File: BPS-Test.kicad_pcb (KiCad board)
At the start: 2 copper layers, 99 x 94 mm, 128 parts, among them J1 Conn_01x02, J10 Conn_01x02, J11 Conn_01x02, J12 Conn_01x02, J13 Conn_01x02, J14 Conn_01x02, J15 Conn_01x02, J16 Conn_01x02, J17 Conn_01x02, J18 Conn_01x02, J19 Conn_01x02, J2 Conn_01x02, J20 Conn_01x02, J21 Conn_01x02, J22 Conn_01x02, J23 Conn_01x07, J24 Conn_01x07, J25 Conn_01x01, J26 Conn_01x01, J3 Conn_01x02, J4 Conn_01x02, J5 Conn_01x02, J6 Conn_01x02, J7 Conn_01x02, J8 Conn_01x02, J9 Conn_01x02, T1 Transformer_1P_1S, T2 Transformer_1P_1S, U1 LM5180QNGURQ1, U2 LM5180QNGURQ1

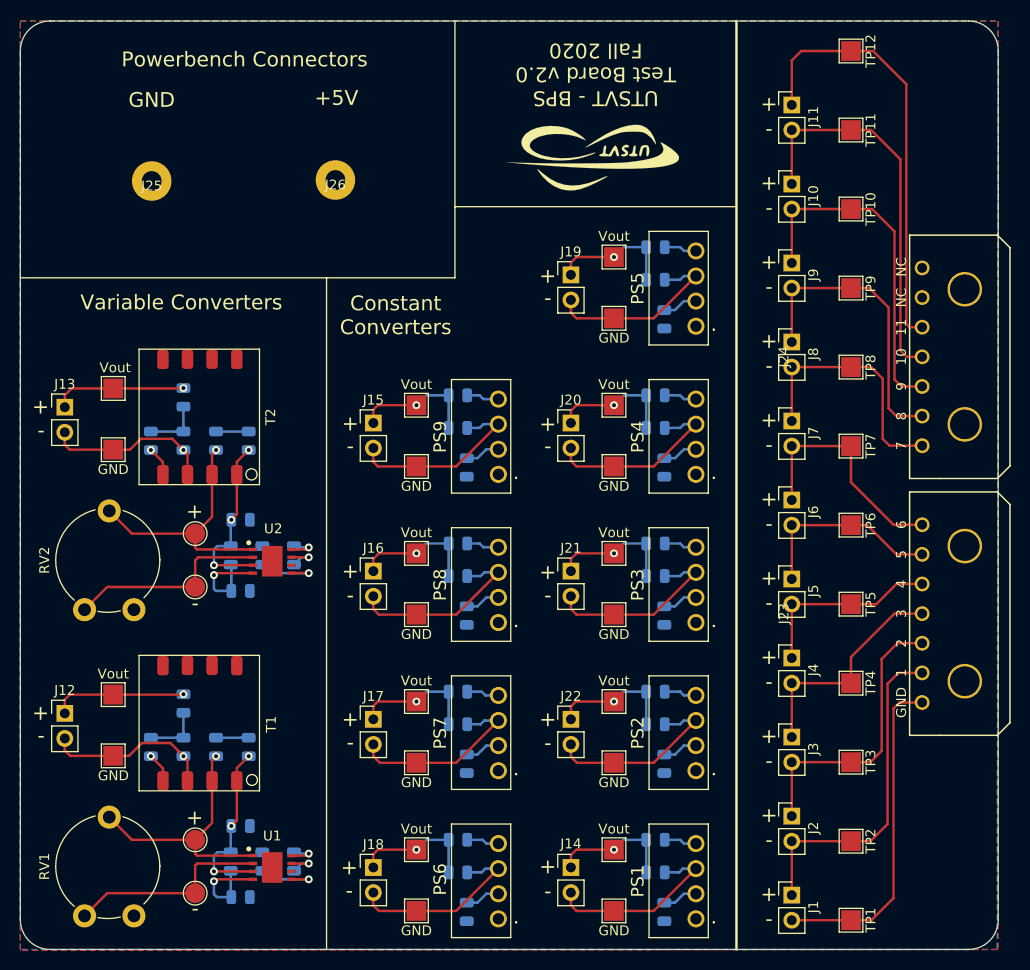
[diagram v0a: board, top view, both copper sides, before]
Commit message: Cleans up repo by adding symbols and footprints to the common library
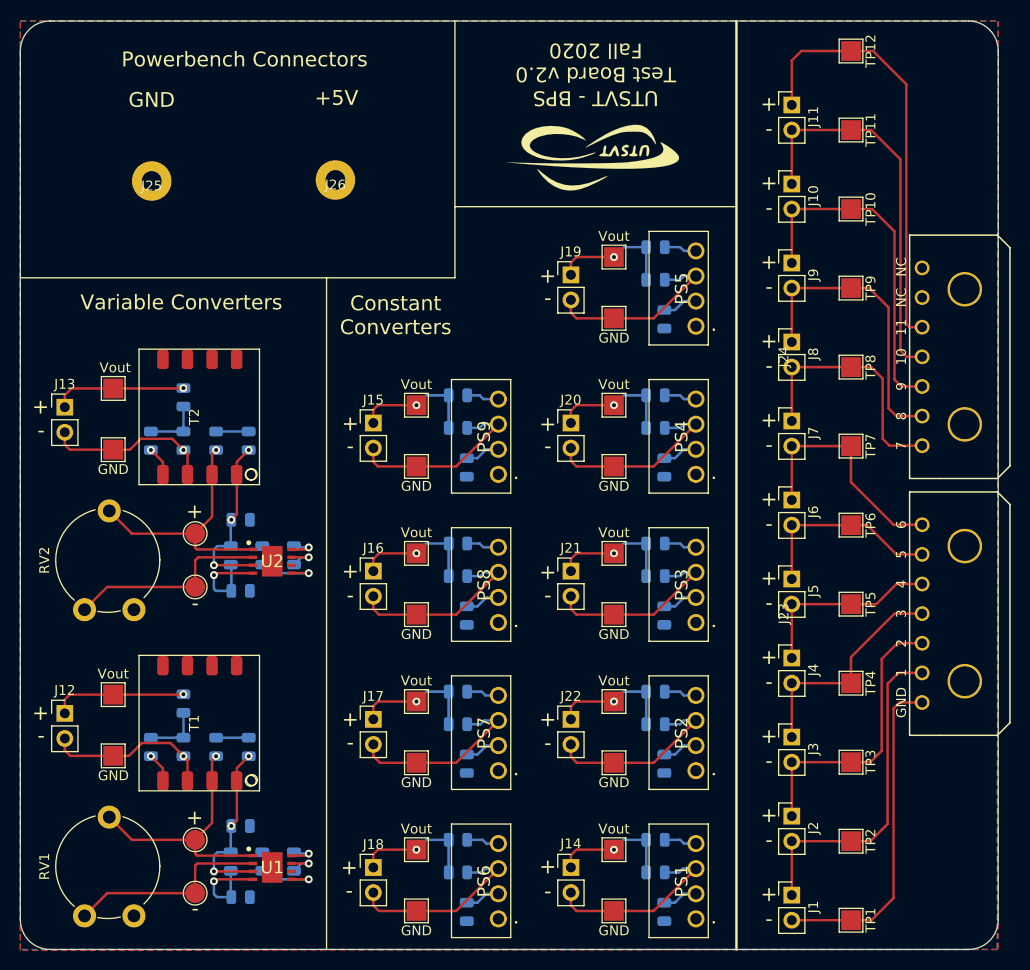
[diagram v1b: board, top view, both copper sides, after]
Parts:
- PS1, PS2, PS3, PS4, PS5, PS6, PS7, PS8, PS9: footprint RFM-5050s:RFM0505S -> UTSVT_Power:RFM0505S
- T1, T2: footprint transformer4:transformer_wuerth_750318463 -> UTSVT_Power:transformer_wuerth_750318463
- U1, U2: footprint LM5180QNGURQ1:SON80P400X400X80-9N -> UTSVT_Power:SON80P400X400X80-9N

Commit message: Adds names
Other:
- board text added: "Aaron, Elijah, Julian, and Siohan were here"
- board text added: "So was Hannah"
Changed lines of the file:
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@@
   (general
     (thickness 1.6)
-    (drawings 108)
+    (drawings 110)
     (tracks 435)
     (zones 0)
@@
   (module UTSVT_Power:transformer_wuerth_750318463 (layer F.Cu)
     (at 109.433 89.926 90)
-    (fp_text reference T2 (at 5.842 3.175 90) (layer F.SilkS)
+    (fp_text reference T2 (at 5.826 10.767 90) (layer F.SilkS)
       (effects (font (size 1 1) (thickness 0.15)))
     )
@@
   (module UTSVT_Power:transformer_wuerth_750318463 (layer F.Cu)
     (at 109.433 120.926 90)
-    (fp_text reference T1 (at 5.842 3.175 90) (layer F.SilkS)
+    (fp_text reference T1 (at 5.826 10.767 90) (layer F.SilkS)
       (effects (font (size 1 1) (thickness 0.15)))
     )
@@
     )
   )
+  (gr_text "So\nwas\nHannah" (at 113 115.1) (layer F.SilkS)
+    (effects (font (size 1 1) (thickness 0.15)))
+  )
+  (gr_text "Aaron, Elijah,\nJulian, and\nSiohan were\nhere" (at 113.1 84.2) (layer F.SilkS)
+    (effects (font (size 1 1) (thickness 0.15)))
+  )
   (gr_text NC (at 184.2 68.9 90) (layer F.SilkS)
     (effects (font (size 1 1) (thickness 0.15)))
@@
     (effects (font (size 1.5 1.5) (thickness 0.3)))
   )
-  (gr_text Vout (at 104.6 79.1) (layer F.SilkS)
+  (gr_text Vout (at 104.4 79.1) (layer F.SilkS)
     (effects (font (size 1 1) (thickness 0.15)))
   )

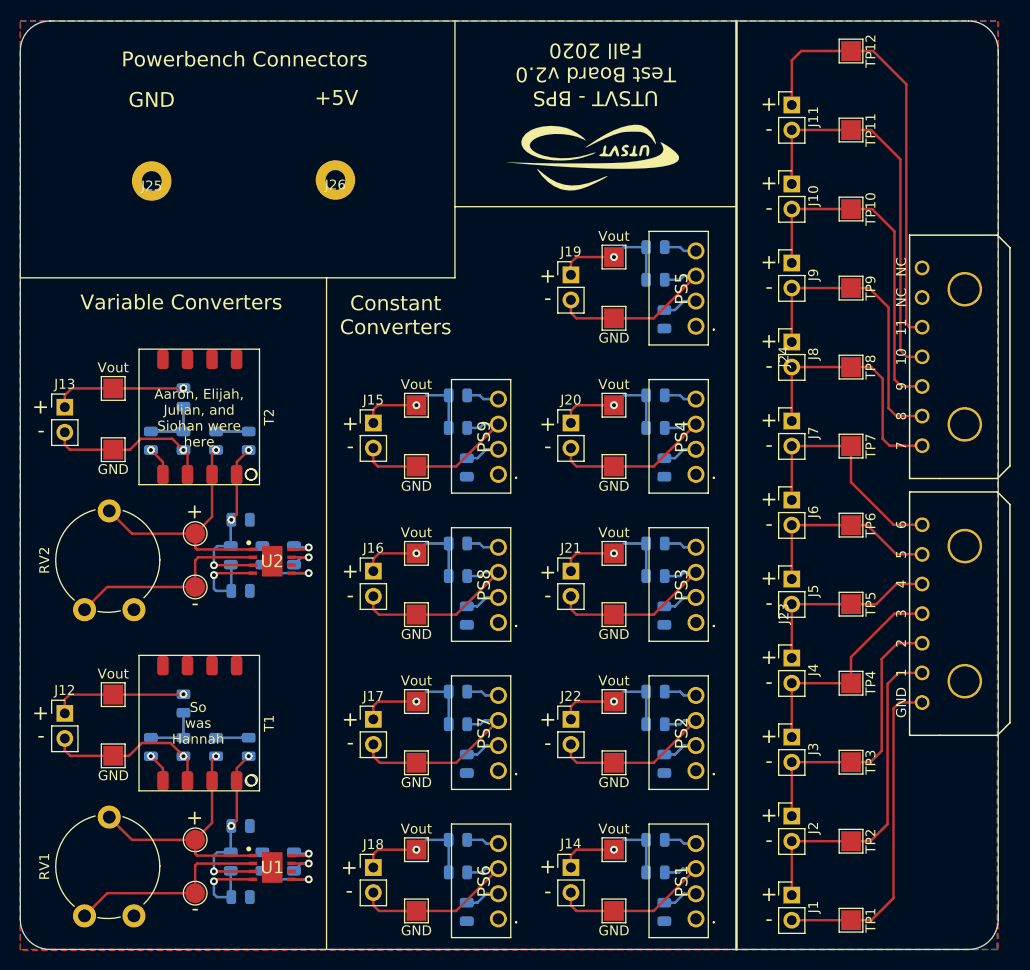
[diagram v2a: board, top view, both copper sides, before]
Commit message: Simplifies variable circuitry and adds gerbers
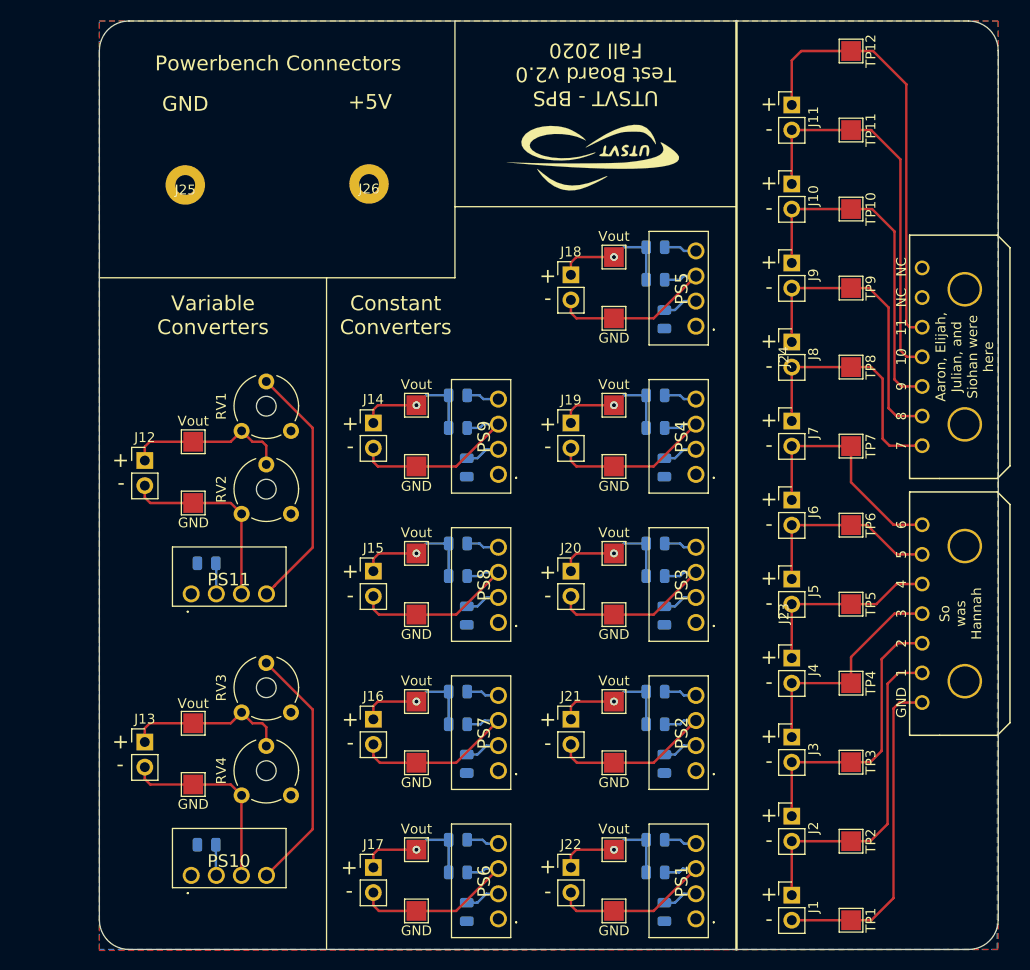
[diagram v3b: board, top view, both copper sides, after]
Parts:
- removed C12: 22n, Capacitor_SMD:C_0805_2012Metric
- removed C13, C14: 500u, Capacitor_SMD:C_0805_2012Metric
- removed C15: 460u, Capacitor_SMD:C_0805_2012Metric
- removed D1, D2: D_Zener, Diode_SMD:D_0805_2012Metric
- removed D3, D4: D, Diode_SMD:D_0805_2012Metric
- removed D5, D6: D_Schottky, Diode_SMD:D_0805_2012Metric
- removed R1, R3: 536k, Resistor_SMD:R_0805_2012Metric
- removed R2, R4: 100k, Resistor_SMD:R_0805_2012Metric
- removed R25, R26: 1k, Resistor_SMD:R_0805_2012Metric
- removed R5, R6: 12.1k, Resistor_SMD:R_0805_2012Metric
- removed T1, T2: Transformer_1P_1S, UTSVT_Power:transformer_wuerth_750318463
- removed TP13: Pot1-TestPoint1, TestPoint:TestPoint_Pad_D2.0mm
- removed TP14: Pot1-TestPoint2, TestPoint:TestPoint_Pad_D2.0mm
- removed TP15: Pot2-TestPoint1, TestPoint:TestPoint_Pad_D2.0mm
- removed TP16: Pot2-TestPoint2, TestPoint:TestPoint_Pad_D2.0mm
- removed U1, U2: LM5180QNGURQ1, UTSVT_Power:SON80P400X400X80-9N
- added PS10: RFM-0505S, UTSVT_Power:RFM0505S, F.Cu at (112.3, 130.5)
- added PS11: RFM-0505S, UTSVT_Power:RFM0505S, F.Cu at (112.3, 102.0)
- added RV3: R_POT, Potentiometer_THT:Potentiometer_Piher_PT-6-V_Vertical_Hole, F.Cu at (122.4, 114.0)
- added RV4: R_POT, Potentiometer_THT:Potentiometer_Piher_PT-6-V_Vertical_Hole, F.Cu at (122.4, 122.4)
- C1: value 460u -> 6.8u
- C11: value 22n -> 6.8u
- RV1, RV2: footprint Potentiometer_THT:Potentiometer_Piher_PT-10-V10_Vertical -> Potentiometer_THT:Potentiometer_Piher_PT-6-V_Vertical_Hole
- moved J18 63.2 mm to (150.7, 69.7)
- moved RV1 51.6 mm to (122.4, 85.5)
- moved J14 49.2 mm to (130.7, 84.7)
- moved J13 34.9 mm to (107.6, 117.0)
- moved TP19 34.9 mm to (112.5, 121.3)
- moved TP20 34.9 mm to (112.5, 115.1)
- moved C11 29.8 mm to (113.9, 127.4), turned to 0 degrees
- moved TP17 26.9 mm to (112.5, 92.8)
- moved TP18 26.9 mm to (112.5, 86.6)
- moved J12 26.9 mm to (107.6, 88.5)
- moved C1 26.8 mm to (113.9, 98.9)
- moved RV2 18.6 mm to (122.4, 93.9)
- moved J15 15.0 mm to (130.7, 99.7)
- moved J16 15.0 mm to (130.7, 114.7)
- moved J19 15.0 mm to (150.7, 84.7)
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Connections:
- C1 pad 1: +5V -> GND
- C1 pad 2: GND -> +5V
- C11 pad 1: Net-(C11-Pad1) -> GND
- C11 pad 2: GND -> +5V
- J12 pad 2: Net-(C14-Pad2) -> Net-(J12-Pad2)
- PS1 pad 3: Net-(J14-Pad2) -> Net-(J22-Pad2)
- PS2 pad 3: Net-(J22-Pad2) -> Net-(J21-Pad2)
- PS3 pad 3: Net-(J21-Pad2) -> Net-(J20-Pad2)
- PS4 pad 3: Net-(J20-Pad2) -> Net-(J19-Pad2)
- PS5 pad 3: Net-(J19-Pad2) -> Net-(J18-Pad2)
- PS6 pad 3: Net-(J18-Pad2) -> Net-(J17-Pad2)
- PS7 pad 3: Net-(J17-Pad2) -> Net-(J16-Pad2)
- PS8 pad 3: Net-(J16-Pad2) -> Net-(J15-Pad2)
- PS9 pad 3: Net-(J15-Pad2) -> Net-(J14-Pad2)
- R10 pad 2: Net-(J19-Pad1) -> Net-(J18-Pad1)
- R11 pad 2: Net-(J18-Pad1) -> Net-(J17-Pad1)
- R12 pad 2: Net-(J17-Pad1) -> Net-(J16-Pad1)
- R13 pad 2: Net-(J16-Pad1) -> Net-(J15-Pad1)
- R14 pad 2: Net-(J15-Pad1) -> Net-(J14-Pad1)
- R15 pad 2: Net-(J14-Pad1) -> Net-(J22-Pad1)
- R16 pad 1: Net-(J22-Pad1) -> Net-(J21-Pad1)
- R16 pad 2: Net-(J22-Pad2) -> Net-(J21-Pad2)
- R17 pad 1: Net-(J21-Pad1) -> Net-(J20-Pad1)
- R17 pad 2: Net-(J21-Pad2) -> Net-(J20-Pad2)
- R18 pad 1: Net-(J20-Pad1) -> Net-(J19-Pad1)
- R18 pad 2: Net-(J20-Pad2) -> Net-(J19-Pad2)
- R19 pad 1: Net-(J19-Pad1) -> Net-(J18-Pad1)
- R19 pad 2: Net-(J19-Pad2) -> Net-(J18-Pad2)
- R20 pad 1: Net-(J18-Pad1) -> Net-(J17-Pad1)
- R20 pad 2: Net-(J18-Pad2) -> Net-(J17-Pad2)
- R21 pad 1: Net-(J17-Pad1) -> Net-(J16-Pad1)
- R21 pad 2: Net-(J17-Pad2) -> Net-(J16-Pad2)
- R22 pad 1: Net-(J16-Pad1) -> Net-(J15-Pad1)
- R22 pad 2: Net-(J16-Pad2) -> Net-(J15-Pad2)
- R23 pad 1: Net-(J15-Pad1) -> Net-(J14-Pad1)
- R23 pad 2: Net-(J15-Pad2) -> Net-(J14-Pad2)
- R24 pad 1: Net-(J14-Pad1) -> Net-(J22-Pad1)
- R24 pad 2: Net-(J14-Pad2) -> Net-(J22-Pad2)
- R7 pad 2: Net-(J22-Pad1) -> Net-(J21-Pad1)
- R8 pad 2: Net-(J21-Pad1) -> Net-(J20-Pad1)
- R9 pad 2: Net-(J20-Pad1) -> Net-(J19-Pad1)
- RV1 pad 3: Net-(RV1-Pad3) -> Net-(J12-Pad1)
- RV2 pad 2: Net-(D3-Pad2) -> Net-(J12-Pad1)
- RV2 pad 3: Net-(RV2-Pad3) -> Net-(J12-Pad2)
- TP17 pad 1: Net-(C14-Pad2) -> Net-(J12-Pad2)
- TP21 pad 1: Net-(J14-Pad2) -> Net-(J22-Pad2)
- TP22 pad 1: Net-(J14-Pad1) -> Net-(J22-Pad1)
- TP23 pad 1: Net-(J15-Pad2) -> Net-(J14-Pad2)
- TP24 pad 1: Net-(J15-Pad1) -> Net-(J14-Pad1)
- TP25 pad 1: Net-(J16-Pad2) -> Net-(J15-Pad2)
- TP26 pad 1: Net-(J16-Pad1) -> Net-(J15-Pad1)
- TP27 pad 1: Net-(J17-Pad2) -> Net-(J16-Pad2)
- TP28 pad 1: Net-(J17-Pad1) -> Net-(J16-Pad1)
- TP29 pad 1: Net-(J18-Pad2) -> Net-(J17-Pad2)
- TP30 pad 1: Net-(J18-Pad1) -> Net-(J17-Pad1)
- TP31 pad 1: Net-(J19-Pad2) -> Net-(J18-Pad2)
- TP32 pad 1: Net-(J19-Pad1) -> Net-(J18-Pad1)
- TP33 pad 1: Net-(J20-Pad2) -> Net-(J19-Pad2)
- TP34 pad 1: Net-(J20-Pad1) -> Net-(J19-Pad1)
- TP35 pad 1: Net-(J21-Pad2) -> Net-(J20-Pad2)
- TP36 pad 1: Net-(J21-Pad1) -> Net-(J20-Pad1)
- TP37 pad 1: Net-(J22-Pad2) -> Net-(J21-Pad2)
- TP38 pad 1: Net-(J22-Pad1) -> Net-(J21-Pad1)
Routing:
- net +5V: track 67.9 -> 38.4 mm, vias 6 -> 0
- net Net-(D3-Pad2): track 26.3 -> 0.00 mm, vias 1 -> 0
- net Net-(PS10-Pad4): track 0.00 -> 25.4 mm
- net Net-(RV1-Pad3): track 20.9 -> 0.00 mm
- net Net-(RV2-Pad3): track 20.8 -> 0.00 mm
- net Net-(J12-Pad2): track 0.00 -> 19.8 mm
- net Net-(C14-Pad2): track 17.4 -> 0.00 mm, vias 1 -> 0
- net Net-(R1-Pad2): track 9.97 -> 0.00 mm, vias 1 -> 0
- net Net-(R3-Pad2): track 9.91 -> 0.00 mm, vias 1 -> 0
- net Net-(C12-Pad1): track 6.81 -> 0.00 mm, vias 1 -> 0
- net Net-(C11-Pad1): track 6.81 -> 0.00 mm, vias 1 -> 0
- net GND: track 6.78 -> 0.00 mm, vias 2 -> 0
- net Net-(C14-Pad1): track 5.83 -> 0.00 mm
- net Net-(C13-Pad1): track 5.83 -> 0.00 mm
- net Net-(R5-Pad1): track 3.56 -> 0.00 mm, vias 1 -> 0
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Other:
- board size 99 x 94 mm -> 91 x 94 mm
